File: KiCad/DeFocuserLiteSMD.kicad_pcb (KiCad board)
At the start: 2 copper layers, 38.1 x 48.3 mm, 22 parts, among them M1 MTR, U1 MOUDLE-SEEEDUINO-XIAO-ESP32C3, U2 MT3608, U3 TMC2209-LA-T

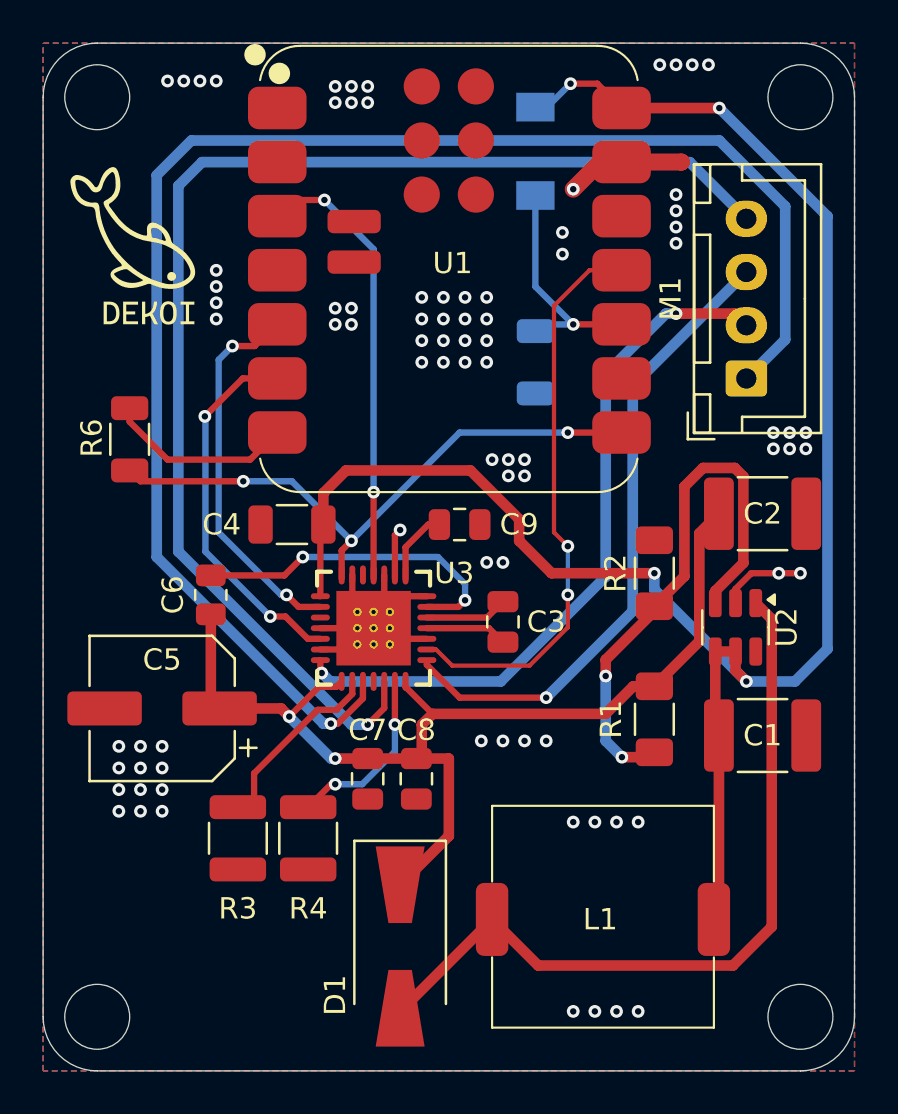
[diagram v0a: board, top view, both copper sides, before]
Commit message: Trying V2 with better pcb layout to expose I2C, and new driver with standalone app integrated as a mediator
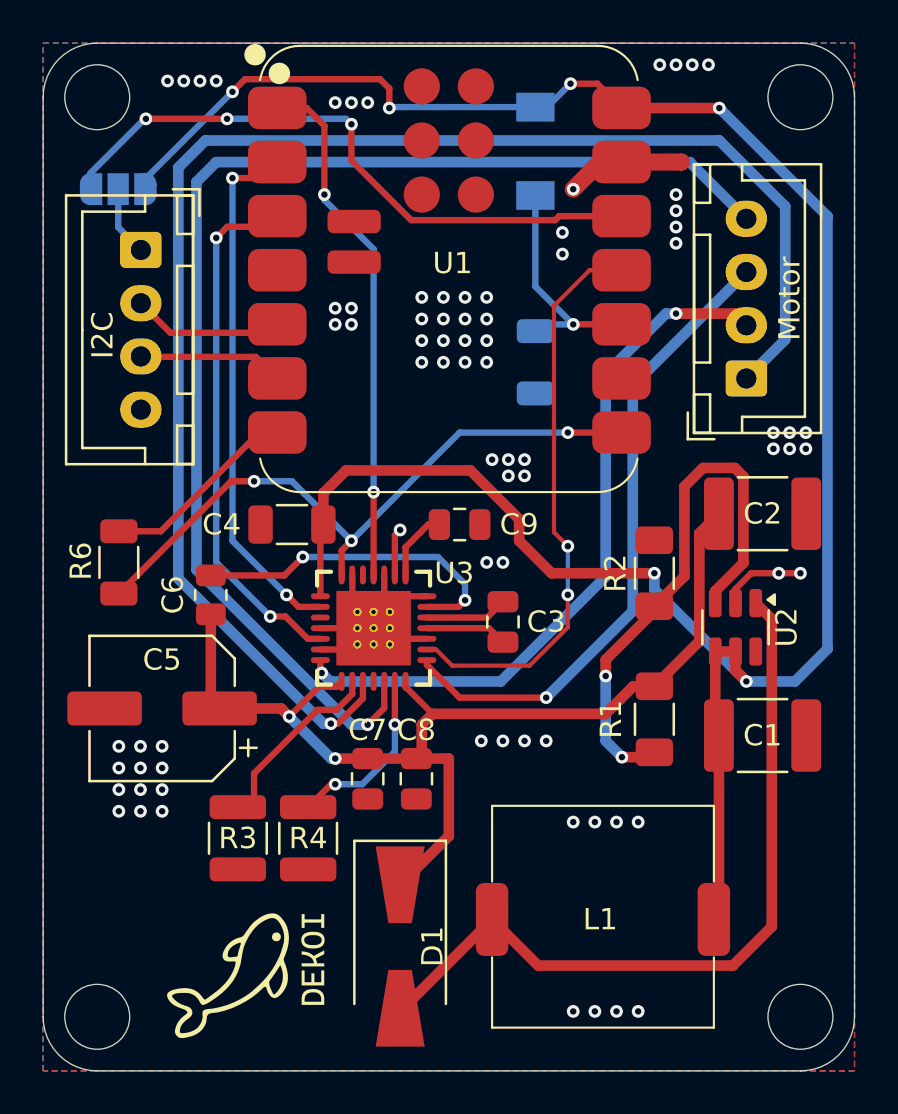
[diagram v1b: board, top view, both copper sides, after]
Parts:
- added I2C: MTR, Connector_JST:JST_XH_B4B-XH-A_1x04_P2.50mm_Vertical, F.Cu at (131.6, 85.9)
- added JP1: SolderJumper_3_Open, Jumper:SolderJumper-3_P1.3mm_Open_RoundedPad1.0x1.5mm_NumberLabels, B.Cu at (130.5, 83.1)
- moved R6 5.80 mm to (130.6, 100.6)
- renumbered M1 to Motor
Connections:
- U1 pad 1: unconnected-(U1-PA02_A0_D0-Pad1) -> DIAG
- U1 pad 12: unconnected-(U1-3V3-Pad12) -> +3.3V
- U1 pad 2: unconnected-(U1-PA4_A1_D1-Pad2) -> STP
- U1 pad 3: DIAG -> DIR
- U1 pad 5: STP -> SDA
- U1 pad 6: DIR -> SCL
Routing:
- net +3.3V: track 0.00 -> 29.8 mm, vias 0 -> 3
- net +5V: track 87.2 -> 109.0 mm, vias 4 -> 6
- net DIR: track 17.6 -> 25.8 mm
- net SDA: track 0.00 -> 7.19 mm
- net STP: track 17.9 -> 25.0 mm
- net SCL: track 0.00 -> 6.83 mm
- net DIAG: track 21.3 -> 24.8 mm
- net Net-(JP1-C): track 0.00 -> 3.29 mm
- net RX: track 28.5 -> 31.0 mm
- net A+: track 72.4 -> 71.2 mm
- net B+: track 60.0 -> 58.9 mm
- net TX: track 8.83 -> 9.36 mm
- net GND: vias 85 -> 78
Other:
- board text added: "3.3v"
- board text added: "5v"
- board text added: "A+"
- board text added: "A-"
- board text added: "B+"
- board text added: "B-"
- board text added: "GND"
- board text added: "SCL"
- board text added: "SDA"
- board text added: "VCC"
